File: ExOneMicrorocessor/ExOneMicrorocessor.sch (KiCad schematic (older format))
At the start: 36 parts, among them IC1 STM32G041C8T6, IC2 FT230XS, J1 UJ2-MBH-3-SMT, J2 Conn_01x02, J3 02x03 Header, J4 01x03, J5 01x08, J6 01x10, J7 01x12, SW1 SW4Push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

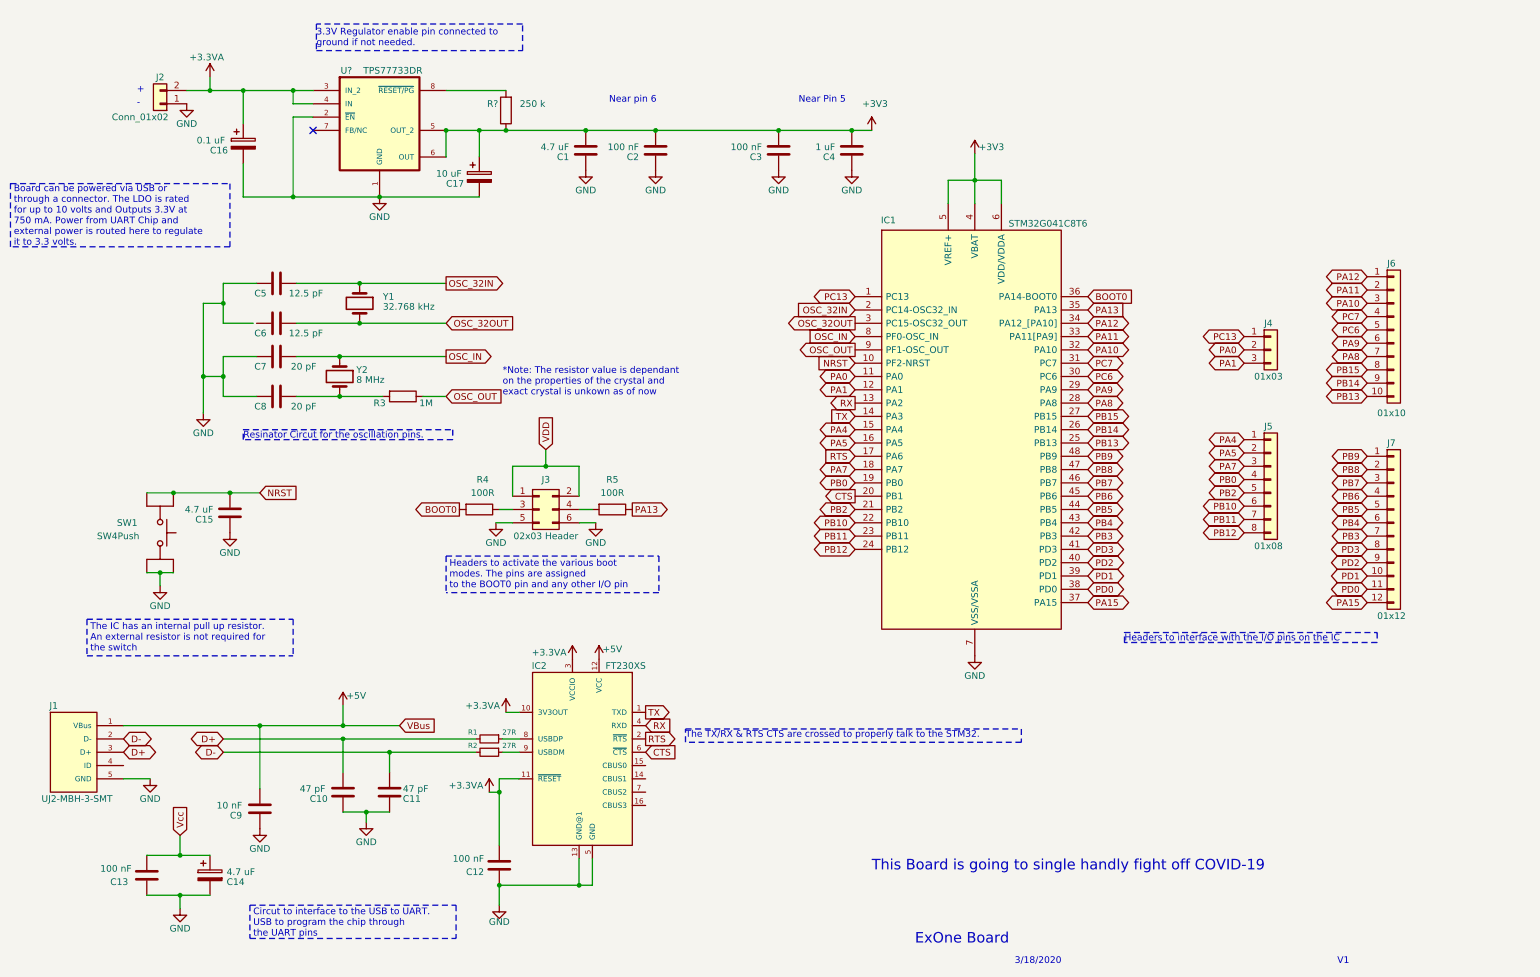
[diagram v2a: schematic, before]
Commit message: Fixed schematic
Change bypass caps on the IC

added pull up resistors on the switch

removed some comments
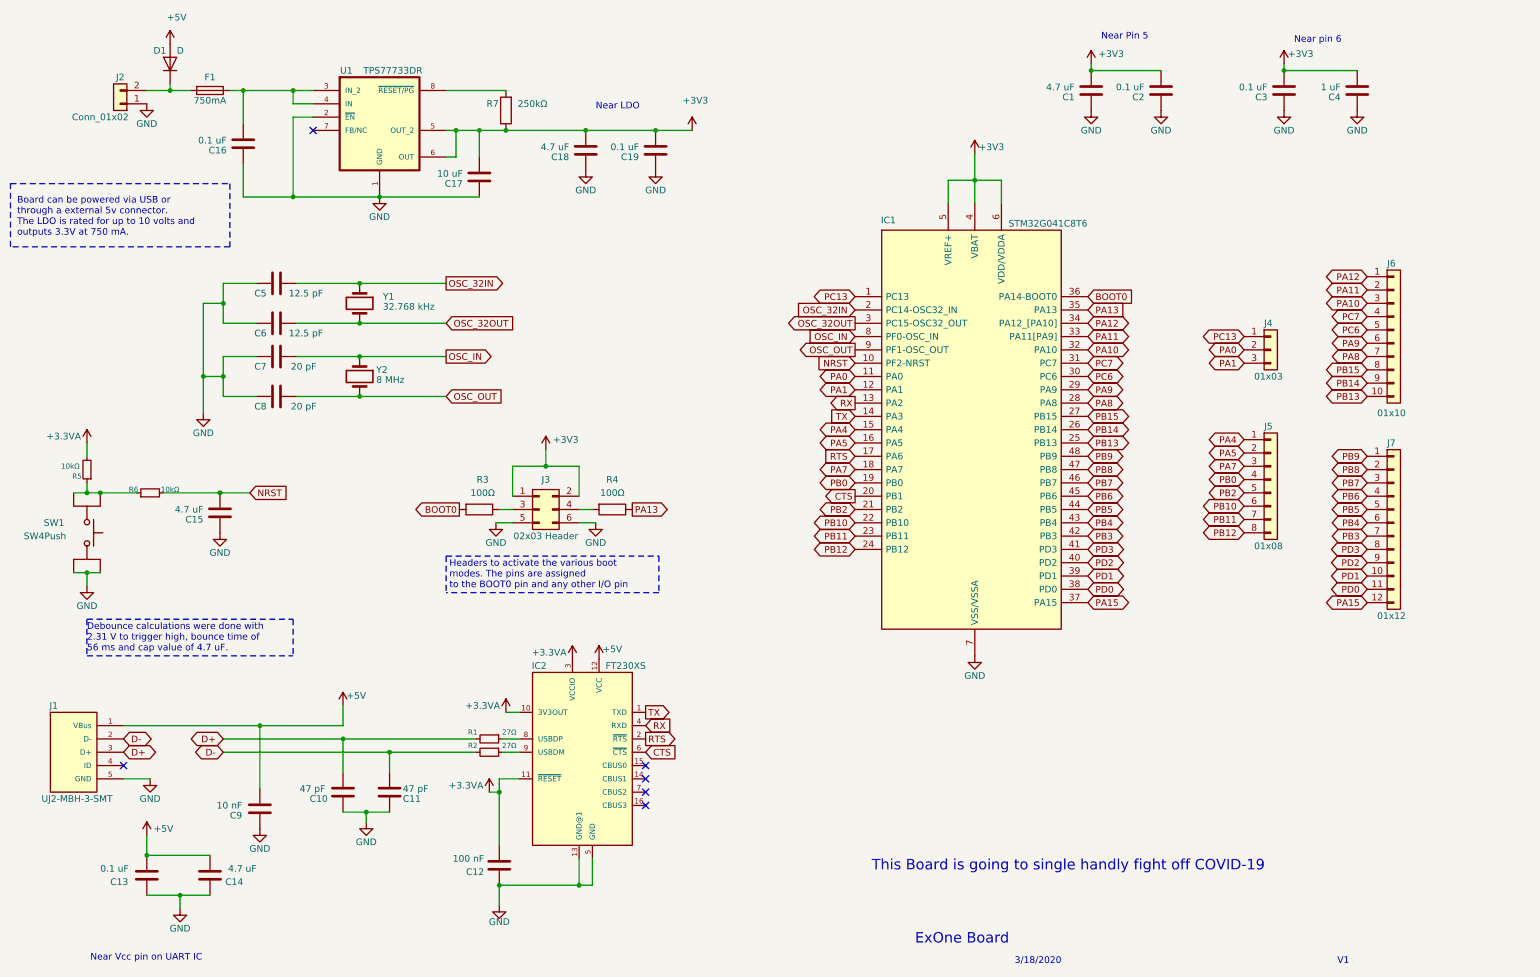
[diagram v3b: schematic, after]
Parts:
- removed C14: 4.7 uF, symbol Device:CP
- removed C16: 0.1 uF, symbol Device:CP
- removed C17: 10 uF, symbol Device:CP
- removed R3: 1M, symbol Device:R
- added C1, C14: 4.7 uF, symbol Device:C
- added C16, C2: 0.1 uF, symbol Device:C
- added C17: 10 uF, symbol Device:C
- added D1: D, symbol Device:D
- added F1: 750mA, symbol Device:Fuse
- added R5, R6: 10kΩ, symbol Device:R_Small
- C13, C3: value 100 nF -> 0.1 uF
- C19: renamed from C2; value 100 nF -> 0.1 uF
- R1, R2: value 27R -> 27Ω
- R3: renamed from R4; value 100R -> 100Ω
- R4: renamed from R5; value 100R -> 100Ω
- R7: renamed from R?; value 250 k -> 250kΩ
- gave numbers to parts that had none: 1
- renumbered C1 to C18
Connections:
- net VDD is gone; now on net +3V3: J3.1 (Pin_1), J3.2 (Pin_2)
- net Vcc is gone; now on net +5V: C13.1
- net +3.3VA: now also R5.2; no longer J2.2 (Pin_2), U1.3 (IN_2), U1.4 (IN)
- net +3V3: now also C1.2, C17.2, C2.2
- net +5V: now also C14.2, D1.2 (A)
- net GND: now also C6.1, C1.1, C14.1, C16.1, C17.1, C2.1
- net NRST: now also R6.2; no longer SW1.2, SW1.3
- net OSC_OUT: now also C8.2, Y2.2
- new net: R5.1, R6.1, SW1.2, SW1.3
- new net: D1.1 (K), F1.2, J2.2 (Pin_2)
- new net: C16.2, F1.1, U1.3 (IN_2), U1.4 (IN)
- no-connect marks 1 -> 6
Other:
- note added: "Board can be powered via USB or\nthrough a external 5v connector.\nThe LDO is rated for up to 10 volts and \noutputs 3.3V at 750 mA."
- note added: "Debounce calculations were done with \n2.31 V to trigger high, bounce time of\n56 ms and cap value of 4.7 uF."
- note added: "Near LDO"
- note added: "Near Vcc pin on UART IC\n"
- note removed: "*Note: The resistor value is dependant\non the properties of the crystal and \nexact crystal is unkown as of now"
- note removed: "+"
- note removed: "-"
- note removed: "3.3V Regulator enable pin connected to\nground if not needed. \n"
- note removed: "Board can be powered via USB or\nthrough a connector. The LDO is rated\nfor up to 10 volts and Outputs 3.3V at\n750 mA. Power from UART Chip and \nexternal power is routed here to regulate\nit to 3.3 volts."
- note removed: "Circut to interface to the USB to UART. \nUSB to program the chip through\nthe UART pins \n\n"
- note removed: "Headers to interface with the I/O pins on the IC"
- note removed: "Resinator Circut for the oscillation pins."
- note removed: "The IC has an internal pull up resistor. \nAn external resistor is not required for \nthe switch"
- note removed: "The TX/RX & RTS CTS are crossed to properly talk to the STM32."
- moved on the sheet: C15, J2, SW1, Y2

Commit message: started work on the PCB layout
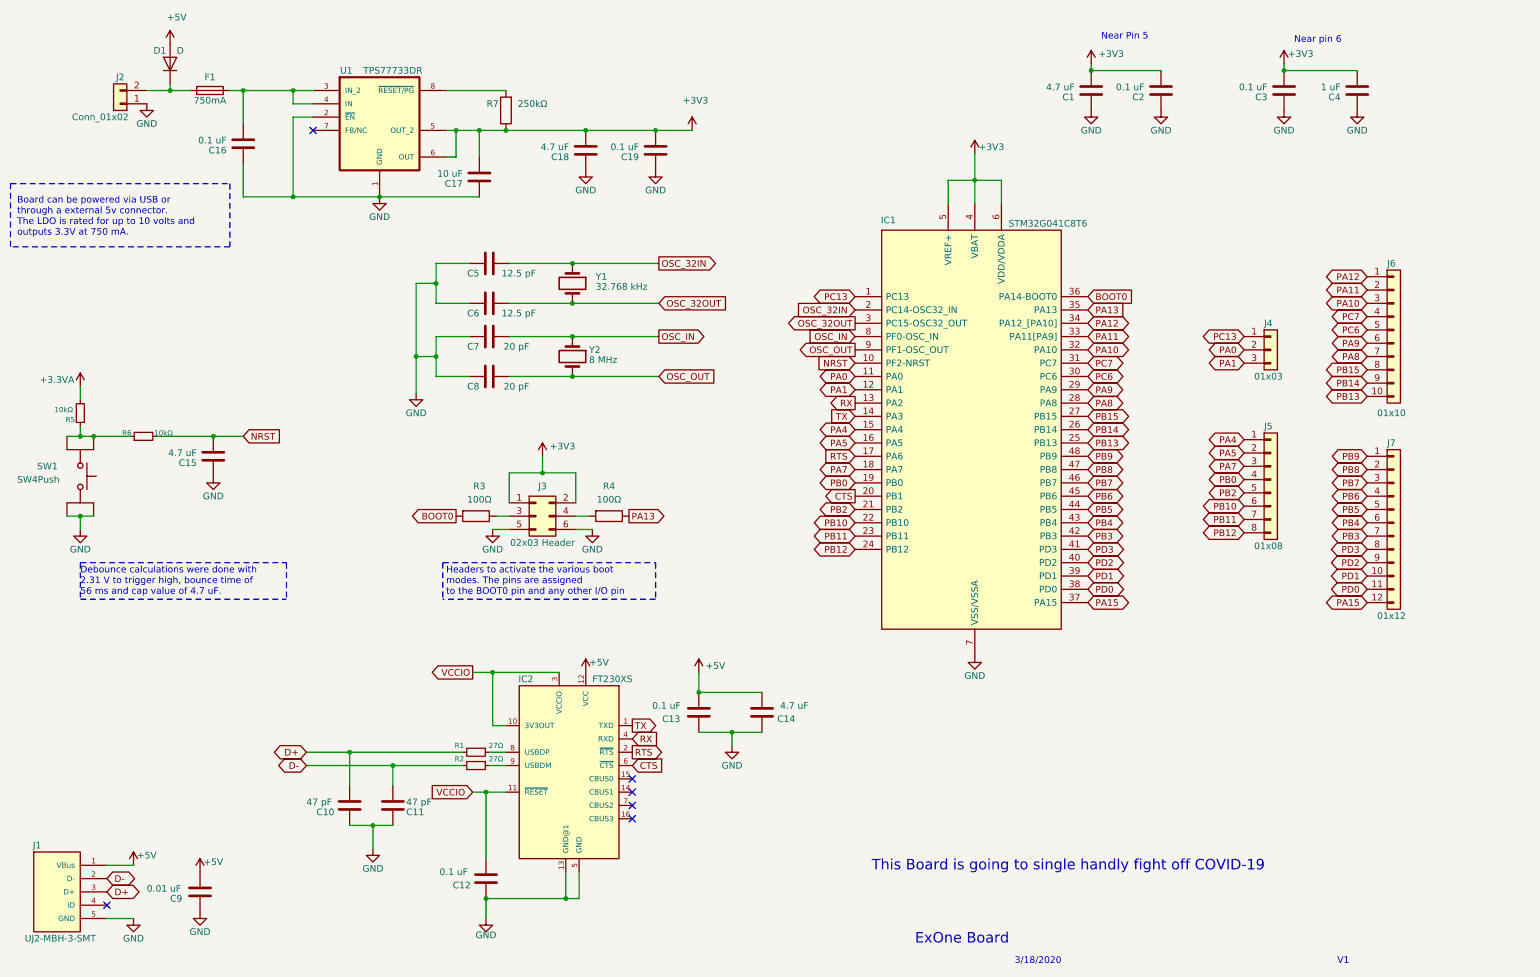
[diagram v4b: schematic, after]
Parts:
- C1, C10, C11, C13, C14, C15, C16, C17, C18, C19, C2, C3, C4, C5, C6, C7, C8: footprint (none) -> Capacitor_SMD:C_0603_1608Metric_Pad1.05x0.95mm_HandSolder
- C12: value 100 nF -> 0.1 uF; footprint (none) -> Capacitor_SMD:C_0603_1608Metric_Pad1.05x0.95mm_HandSolder
- C9: value 10 nF -> 0.01 uF; footprint (none) -> Capacitor_SMD:C_0603_1608Metric_Pad1.05x0.95mm_HandSolder
- D1: footprint (none) -> Diode_SMD:D_SOD-123
- F1: footprint (none) -> Fuse:Fuse_1206_3216Metric_Pad1.42x1.75mm_HandSolder
- IC1: footprint QFP50P900X900X160-48N -> ExOneFootprints:STM32G041C8
- IC2: footprint SSOP16 -> ExOneFootprints:FT230XS
- J1: footprint CUI_UJ2-MBH-3-SMT -> ExOneFootprints:UJ2-MBH-SMT
- J2: footprint (none) -> Connector_JST:JST_EH_B2B-EH-A_1x02_P2.50mm_Vertical
- J3: footprint (none) -> Connector_PinHeader_2.54mm:PinHeader_2x03_P2.54mm_Vertical
- J4: footprint (none) -> Connector_PinHeader_2.54mm:PinHeader_1x03_P2.54mm_Vertical
- J5: footprint (none) -> Connector_PinHeader_2.54mm:PinHeader_1x08_P2.54mm_Vertical
- J6: footprint (none) -> Connector_PinHeader_2.54mm:PinHeader_1x10_P2.54mm_Vertical
- J7: footprint (none) -> Connector_PinHeader_2.54mm:PinHeader_1x12_P2.54mm_Vertical
- R1, R2, R3, R4, R5, R6, R7: footprint (none) -> Resistor_SMD:R_0603_1608Metric_Pad1.05x0.95mm_HandSolder
- SW1: footprint (none) -> Button_Switch_THT:SW_PUSH_6mm
- U1: footprint SOIC127P600X175-8N -> ExOneFootprints:TPS77733
- Y1: footprint (none) -> Crystal:Crystal_SMD_3215-2Pin_3.2x1.5mm
- Y2: footprint (none) -> Crystal:Crystal_SMD_HC49-SD_HandSoldering
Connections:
- net +3.3VA: no longer C12.1, IC2.10 (3V3OUT), IC2.11 (~RESET~), IC2.3 (VCCIO)
- new net VCCIO: C12.1, IC2.10 (3V3OUT), IC2.11 (~RESET~), IC2.3 (VCCIO)
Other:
- note removed: "Near LDO"
- note removed: "Near Vcc pin on UART IC\n"
- moved on the sheet: C10, C11, C12, C13, C14, C15, C5, C6, C7, C8, C9, IC2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
